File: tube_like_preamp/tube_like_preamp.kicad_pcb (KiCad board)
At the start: 2 copper layers, 75.2 x 50.4 mm, 51 parts, among them J1 IN, J2 OUT, J3 Conn_01x02, Q1 BS170, Q2 BC109, Q3 BS170, Q4 BS170, Q5 BC109, Q6 BS170

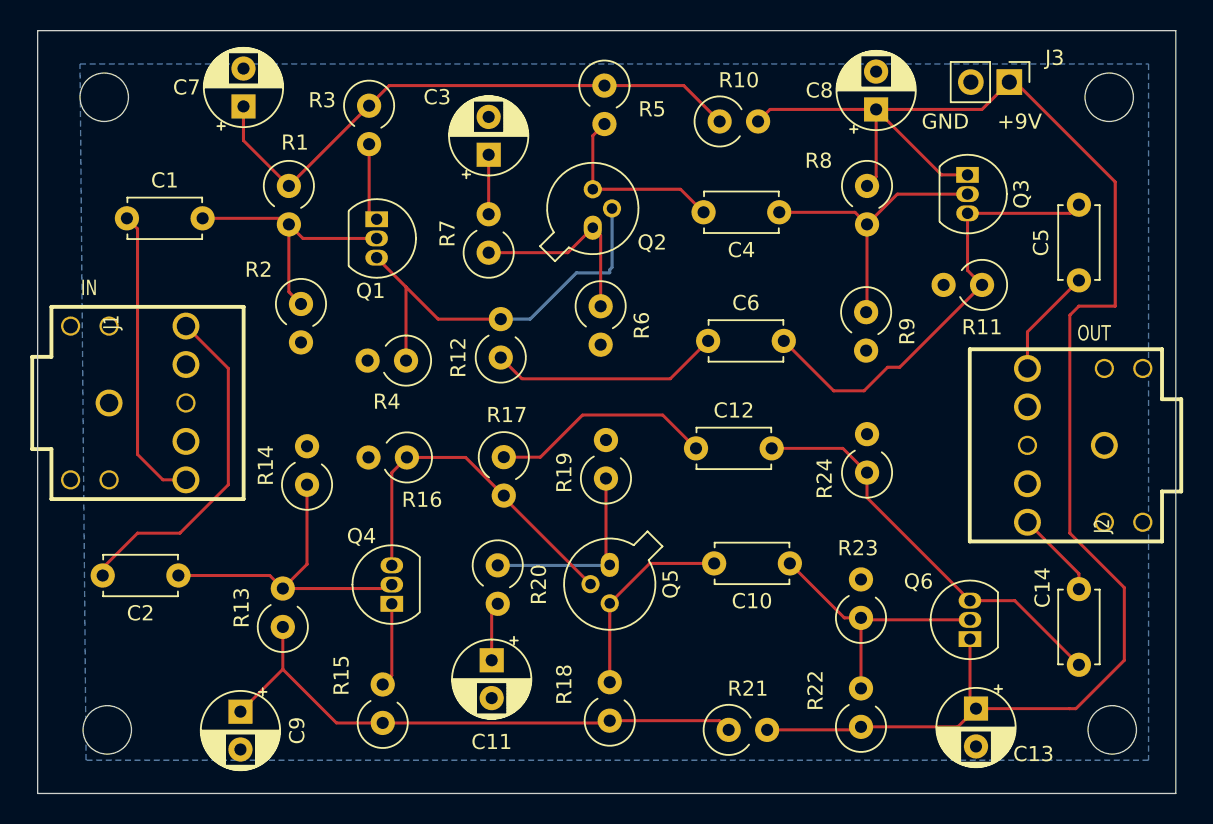
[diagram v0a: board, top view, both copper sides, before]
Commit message: Improve Tube-Like Preamp
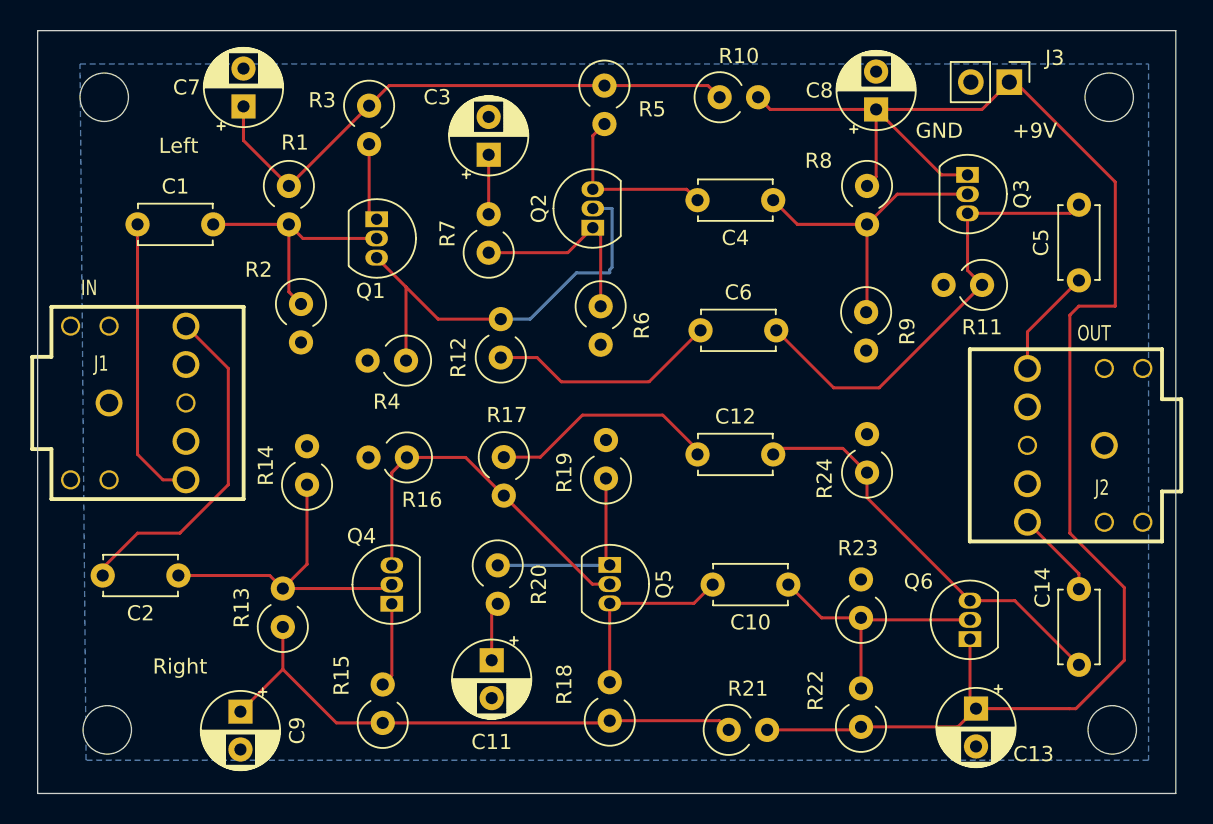
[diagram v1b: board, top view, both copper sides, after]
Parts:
- Q2, Q5: value BC109 -> 2N5088; footprint Package_TO_SOT_THT:TO-18-3 -> Package_TO_SOT_THT:TO-92_Inline
- moved R10 1.60 mm to (156.7, 62.4)
- moved C10 1.40 mm to (161.2, 94.6)
- moved C4 0.89 mm to (160.2, 69.2)
- moved C6 0.86 mm to (155.4, 77.8)
- moved C1 0.81 mm to (118.2, 70.8)
- moved C12 0.41 mm to (155.2, 86.0)
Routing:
- net Net-(Q4-S): track 23.2 -> 24.5 mm
- net Net-(Q1-S): track 27.5 -> 28.8 mm
- net Net-(Q2-C): track 12.6 -> 11.8 mm
- net Net-(Q3-G): track 19.4 -> 20.2 mm
- net Net-(J1-L): track 19.8 -> 19.1 mm
- net Net-(Q5-C): track 13.2 -> 12.5 mm
- net Net-(C7-Pad1): track 38.7 -> 38.0 mm
- net Net-(Q3-S): track 30.1 -> 30.7 mm
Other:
- board text added: "Left"
- board text added: "Right"
- board text added: "https://github.com/jonronen/kicad-stuff"
